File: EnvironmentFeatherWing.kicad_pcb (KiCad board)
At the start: 2 copper layers, 50.8 x 22.9 mm, 19 parts, among them J1 FeatherWing, Q1 BSS138, Q2 BSS138, U1 SHT31-D, U2 MCP1754S-1802xCB, U3 SGP30

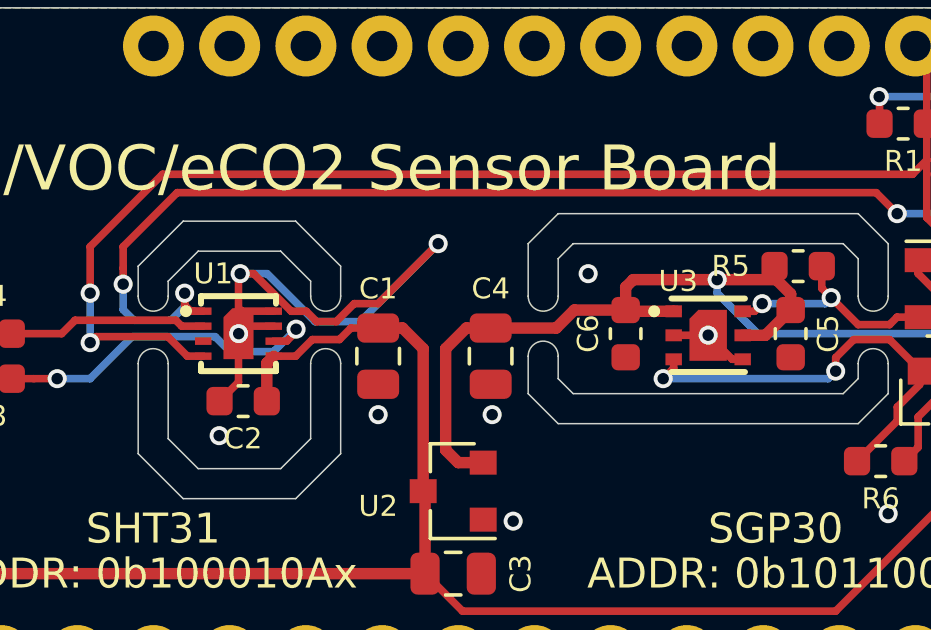
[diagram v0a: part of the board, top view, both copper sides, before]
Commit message: Added missing library cache file
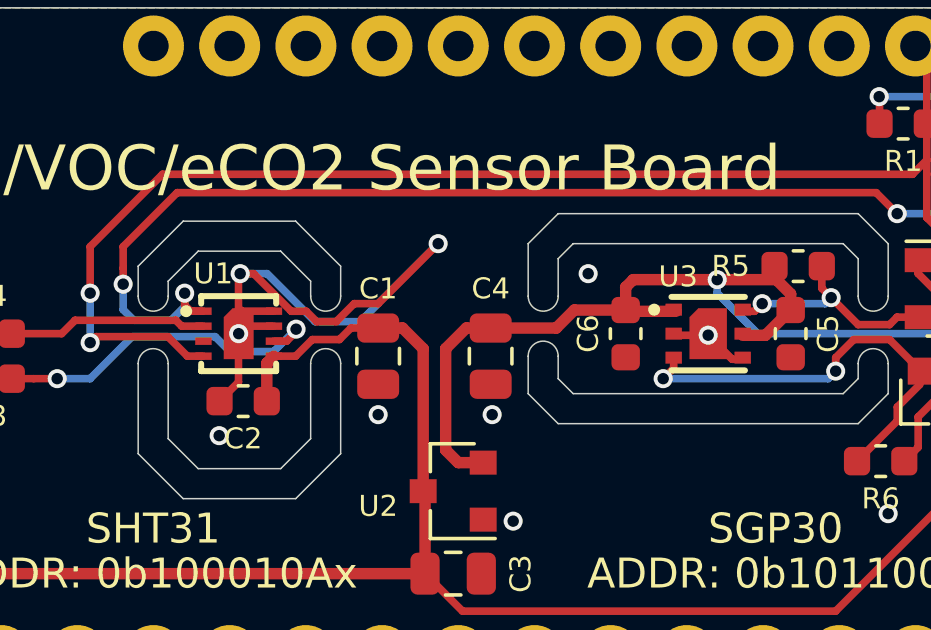
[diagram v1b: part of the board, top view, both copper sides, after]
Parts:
- moved U3 0.05 mm to (157.9, 93.9)
